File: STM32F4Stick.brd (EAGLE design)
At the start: 46.7 x 25.9 mm, 42 parts, among them U1 MIC5219 3.3V, U2 USD-SOCKETNEW

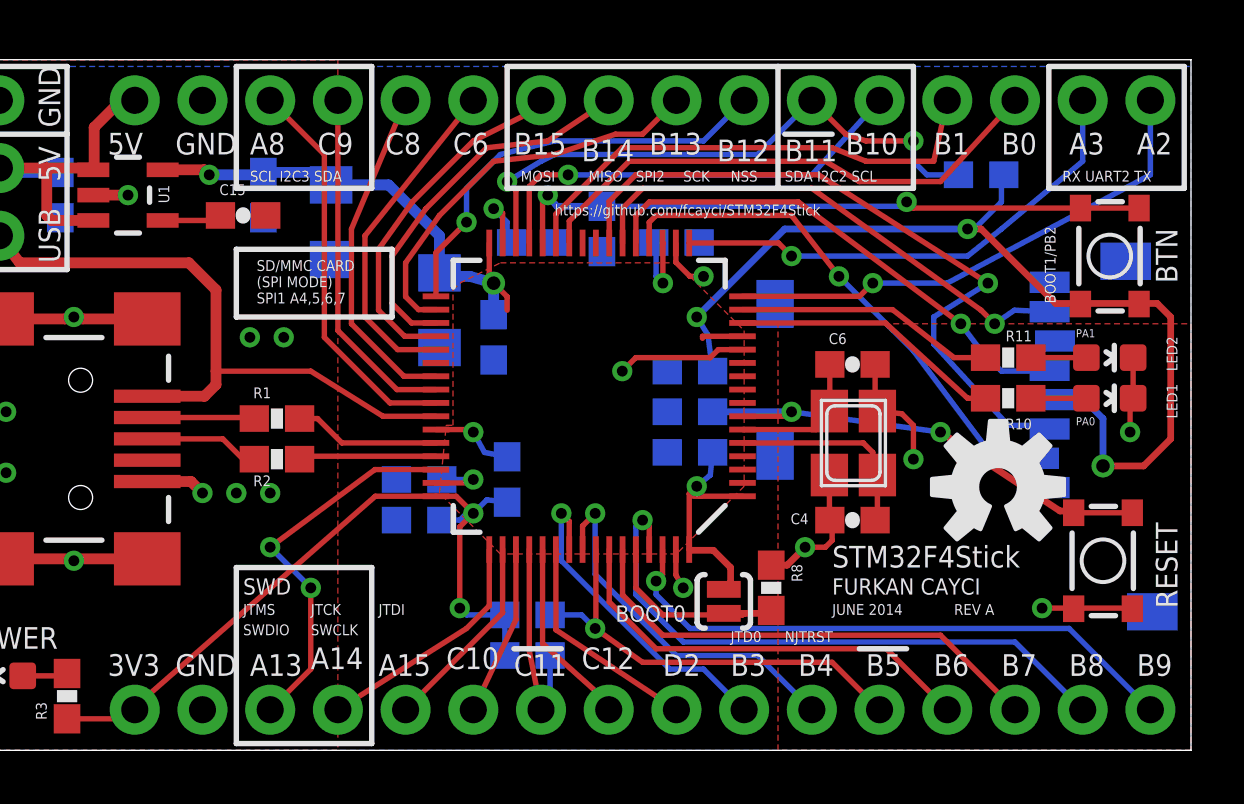
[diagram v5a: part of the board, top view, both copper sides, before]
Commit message: Final Rev B. Added nRF24L01+ 2.4GHz radio compatible header. Got rid of some of the extension headers. Check out RevA if you do not need to use nRF24L01+ radio but instead have extension headers.
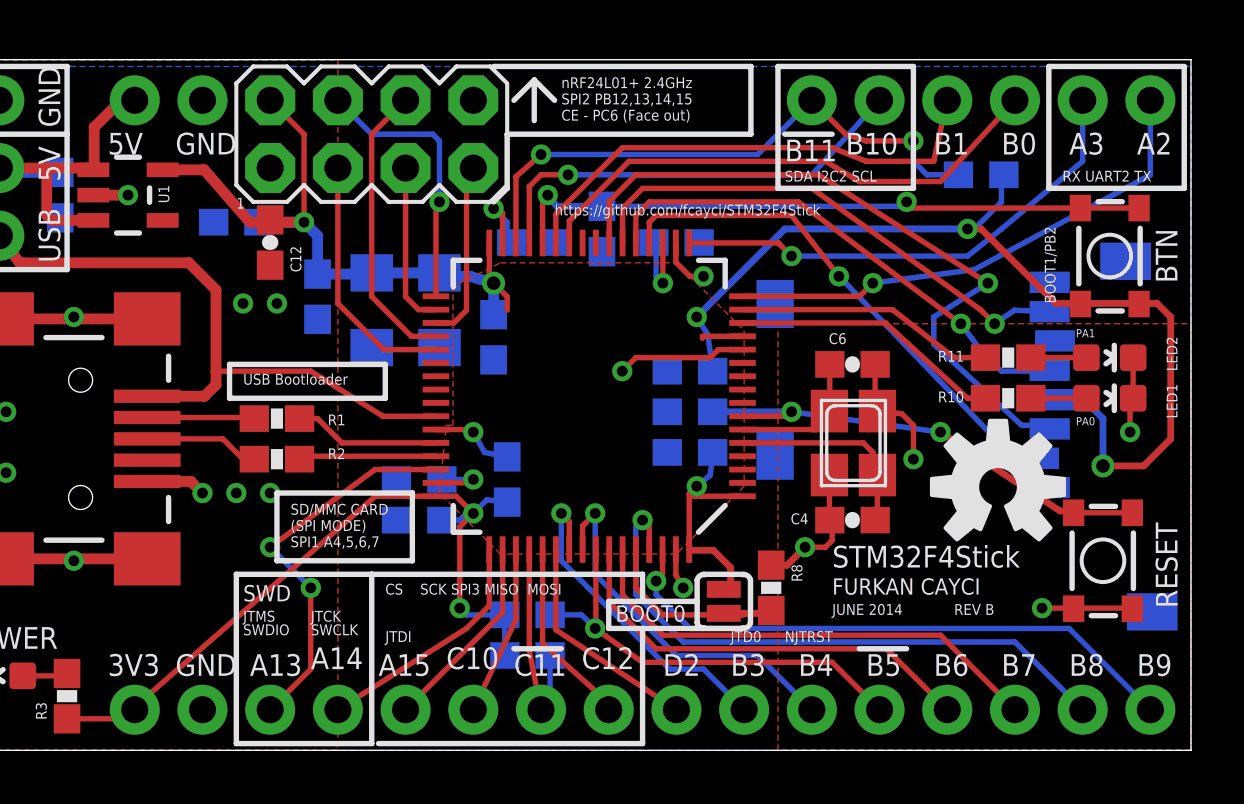
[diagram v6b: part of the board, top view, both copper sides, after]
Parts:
- added -3: M04X2, SparkFun-Connectors:2X4
- added C16: 0.1uF, SparkFun-Capacitors:0603-CAP
- added JP4: M021X02_NO_SILK, SparkFun-Connectors:1X02_NO_SILK
- C12: value 4.7uF -> 1.0uF; device SparkFun-Capacitors:EIA3216 -> SparkFun-Capacitors:0603-CAP
- C13: value 2.2uF -> 0.1uF
- C14: value 0.1uF -> 4.7uF; device SparkFun-Capacitors:0603-CAP -> SparkFun-Capacitors:EIA3216
- C15: value 0.1uF -> 2.2uF
- JP3: value M161X16_NO_SILK -> (none); device SparkFun-Connectors:1X16_NO_SILK -> SparkFun-Connectors:1X06_NO_SILK
- moved JP3 25.4 mm to (32.5, 24.4)
- moved C10 14.2 mm to (14.0, 17.0), turned to 270 degrees
- moved C15 11.9 mm to (17.8, 10.2), flipped to the bottom
- moved C13 10.2 mm to (27.9, 11.2)
- moved C14 10.1 mm to (18.5, 16.5), turned to 90 degrees
- moved C12 6.84 mm to (12.2, 19.1), flipped to the top, turned to 270 degrees
- moved C3 3.64 mm to (16.0, 16.5)
- moved C11 3.05 mm to (27.9, 14.2)
- moved C2 1.44 mm to (10.9, 19.8), turned to 0 degrees
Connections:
- removed net N$2: C15.1, U1.4
- removed net P33: -2.33, JP3.10
- removed net P34: -2.34, JP3.9
- removed net P35: -2.35, JP3.8
- removed net P36: -2.36, JP3.7
- removed net P37: -2.37, JP3.6
- removed net P39: -2.39, JP3.5
- removed net P40: -2.40, JP3.4
- removed net P41: -2.41, JP3.3
- new net RF_CE: -2.37, -3.3
- new net RF_CS: -2.33, -3.4
- new net RF_MISO: -2.35, -3.7
- new net RF_MOSI: -2.36, -3.6
- new net RF_SCK: -2.34, -3.5
- net 5V: now also JP4.1; no longer JP3.1
- net GND: now also -3.1, C12.2, C14.C, C16.2, JP4.2; no longer C12.C, C14.2, JP3.2
- net N$10: now also C15.1; no longer C13.1
- net NRST: now also C16.1; no longer C14.1
- net P16: now also JP3.6; no longer JP3.16
- net P17: now also JP3.5; no longer JP3.15
- net P26: now also JP3.4; no longer JP3.14
- net P27: now also JP3.3; no longer JP3.13
- net P29: now also JP3.2; no longer JP3.12
- net P30: now also JP3.1; no longer JP3.11
- net VCC: now also -3.2, C12.1, C13.1, C14.A; no longer C12.A
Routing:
- net P33: track 16.2 -> 0.00 mm, vias 1 -> 0
- net P34: track 15.2 -> 0.00 mm
- net P41: track 14.9 -> 0.00 mm
- net P35: track 14.2 -> 0.00 mm
- net P36: track 13.4 -> 0.00 mm
- net P40: track 13.2 -> 0.00 mm
- net P39: track 12.8 -> 0.00 mm
- net P37: track 12.7 -> 0.00 mm
- net RF_MOSI: track 0.00 -> 10.9 mm
- net RF_CS: track 0.00 -> 10.3 mm, vias 0 -> 1
- net RF_CE: track 0.00 -> 9.48 mm
- net VCC: track 99.2 -> 106.2 mm
- net RF_MISO: track 0.00 -> 6.78 mm
- net RF_SCK: track 0.00 -> 6.17 mm
- net N$2: track 2.36 -> 0.00 mm
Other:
- board text added: "1"
- board text added: "CS SCK SPI3 MISO MOSI"
- board text added: "REV B"
- board text added: "USB Bootloader"
- board text added: "nRF24L01+ 2.4GHz SPI2 PB12,13,14,15 CE - PC6 (Face out)"
- board text removed: "A8"
- board text removed: "B12"
- board text removed: "B13"
- board text removed: "B14"
- board text removed: "B15"
- board text removed: "C6"
- board text removed: "C8"
- board text removed: "C9"
- board text removed: "MISO"
- board text removed: "MOSI"
- board text removed: "NSS"
- board text removed: "REV A"
- board text removed: "SCK"
- board text removed: "SCL I2C3 SDA"
- board text removed: "SPI2"

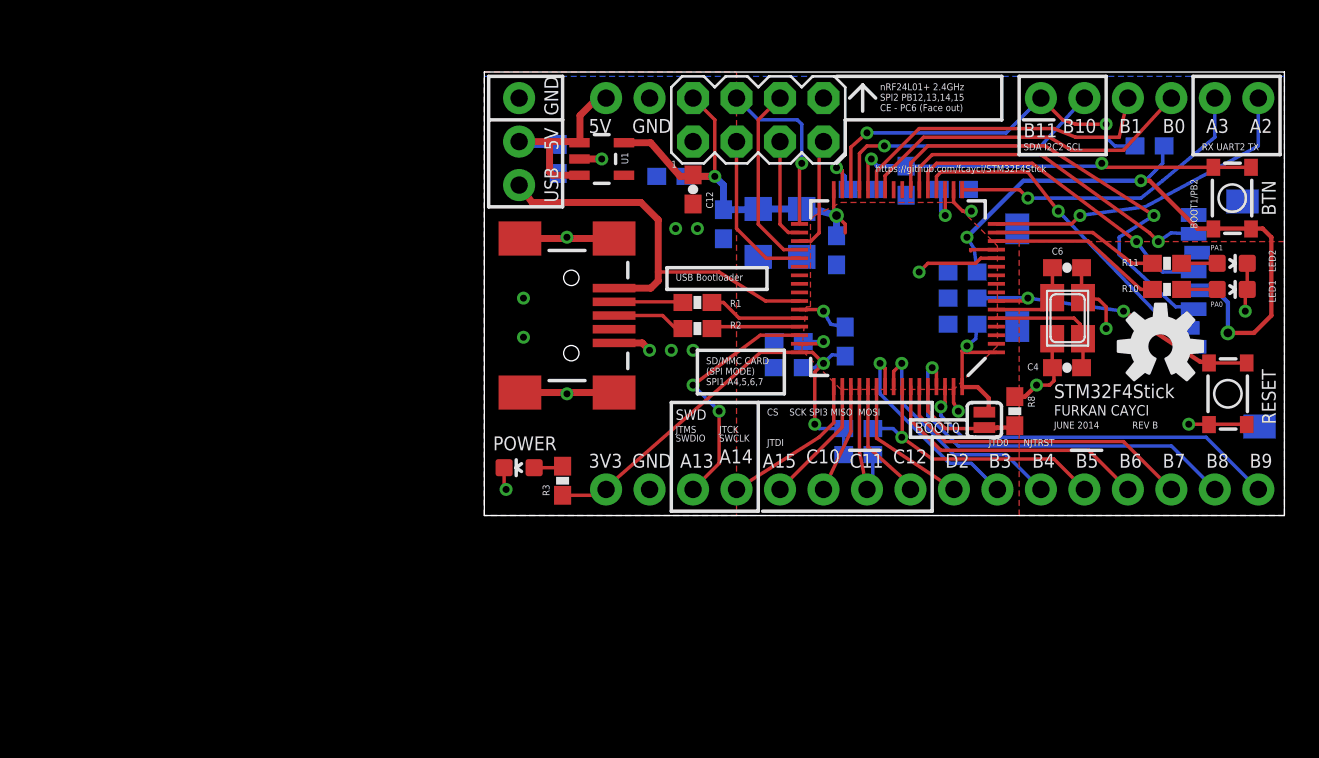
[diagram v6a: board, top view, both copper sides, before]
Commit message: adeed STM32F401 chip support to schematic only
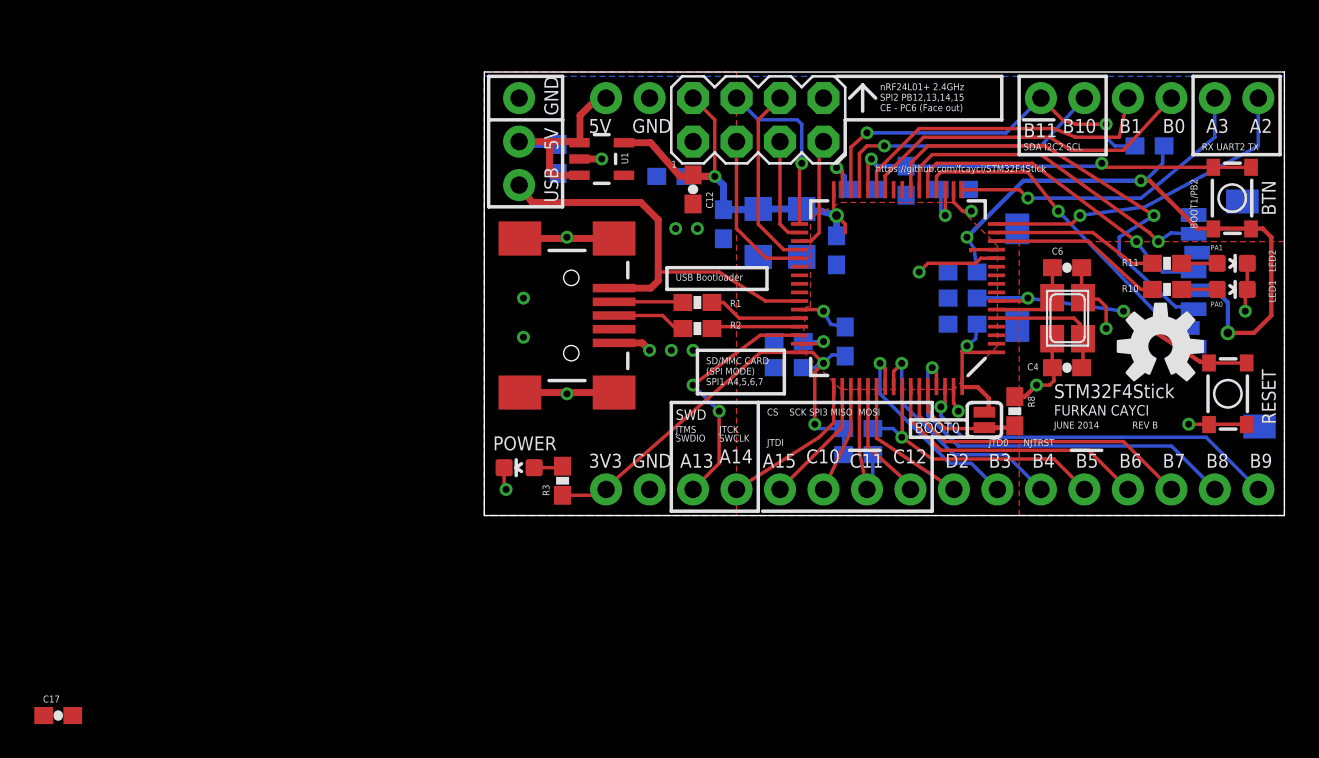
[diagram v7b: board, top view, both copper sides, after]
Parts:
- added C17: 4.7uF, SparkFun-Capacitors:0603-CAP
- C4, C6: value 12pF -> 20pF
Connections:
- net GND: now also C17.2
- net P30: now also C17.1
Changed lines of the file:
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@@
 <text x="16.51" y="5.842" size="0.4064" layer="21" ratio="15">CS    SCK SPI3 MISO  MOSI</text>
 <wire x1="28.448" y1="6.604" x2="29.972" y2="6.604" width="0.2032" layer="21"/>
-<wire x1="28.448" y1="4.572" x2="28.702" y2="4.572" width="0.2032" layer="21"/>
-<wire x1="28.702" y1="4.572" x2="29.972" y2="4.572" width="0.2032" layer="21"/>
-<wire x1="28.448" y1="4.572" x2="26.162" y2="4.572" width="0.2032" layer="21"/>
+<wire x1="29.972" y1="4.572" x2="26.162" y2="4.572" width="0.2032" layer="21"/>
 <wire x1="26.162" y1="5.588" x2="28.194" y2="5.588" width="0.2032" layer="21"/>
 <wire x1="26.162" y1="5.588" x2="24.892" y2="5.588" width="0.2032" layer="21"/>
@@
 <attribute name="VALUE" x="28.956" y="10.033" size="0.4064" layer="28" font="vector" rot="MR0"/>
 </element>
-<element name="C6" library="SparkFun-Capacitors" package="0603-CAP" value="12pF" x="34.036" y="14.478">
+<element name="C6" library="SparkFun-Capacitors" package="0603-CAP" value="20pF" x="34.036" y="14.478">
 <attribute name="PROD_ID" value="CAP-09137" x="92.456" y="-31.242" size="1.778" layer="27" display="off"/>
 </element>
-<element name="C4" library="SparkFun-Capacitors" package="0603-CAP" value="12pF" x="34.036" y="8.636" smashed="yes" rot="R180">
+<element name="C4" library="SparkFun-Capacitors" package="0603-CAP" value="20pF" x="34.036" y="8.636" smashed="yes" rot="R180">
 <attribute name="PROD_ID" value="CAP-09137" x="18.796" y="58.166" size="1.778" layer="27" rot="R180" display="off"/>
 <attribute name="NAME" x="32.385" y="8.89" size="0.4064" layer="25" font="vector" rot="R180"/>
@@
 <attribute name="NAME" x="12.954" y="18.923" size="0.4064" layer="25" font="vector" rot="R270"/>
 <attribute name="VALUE" x="11.049" y="20.066" size="0.4064" layer="27" font="vector" rot="R270"/>
+</element>
+<element name="C17" library="SparkFun-Capacitors" package="0603-CAP" value="4.7uF" x="-24.892" y="-11.684">
+<attribute name="PROD_ID" value="CAP-08280" x="-24.892" y="-11.684" size="1.778" layer="27" ratio="15" display="off"/>
 </element>
 </elements>
@@
 <contactref element="C10" pad="2"/>
 <contactref element="C12" pad="2"/>
+<contactref element="C17" pad="2"/>
+<wire x1="1.155" y1="1.639" x2="-24.042" y2="-11.684" width="0" layer="19" extent="1-1"/>
 </signal>
 <signal name="N$10">
@@
 <wire x1="36.83" y1="21.59" x2="38.012" y2="21.59" width="0.2032" layer="16"/>
 <contactref element="JP3" pad="1"/>
+<contactref element="C17" pad="1"/>
+<wire x1="-25.742" y1="-11.684" x2="21.4108125" y2="19.03239375" width="0" layer="19" extent="1-1"/>
 </signal>
 <signal name="RF_CE">
